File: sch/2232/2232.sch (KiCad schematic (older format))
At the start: 69 parts, among them J1 47346-0001, J2 IDC-06, J3 IDC-06, J4 IDC-10, J5 IDC-10, J6 6P6C, J7 Screw_Terminal_01x06, J8 Screw_Terminal_01x06, Q1 Q_NPN_BEC, Q2 Q_NPN_BEC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

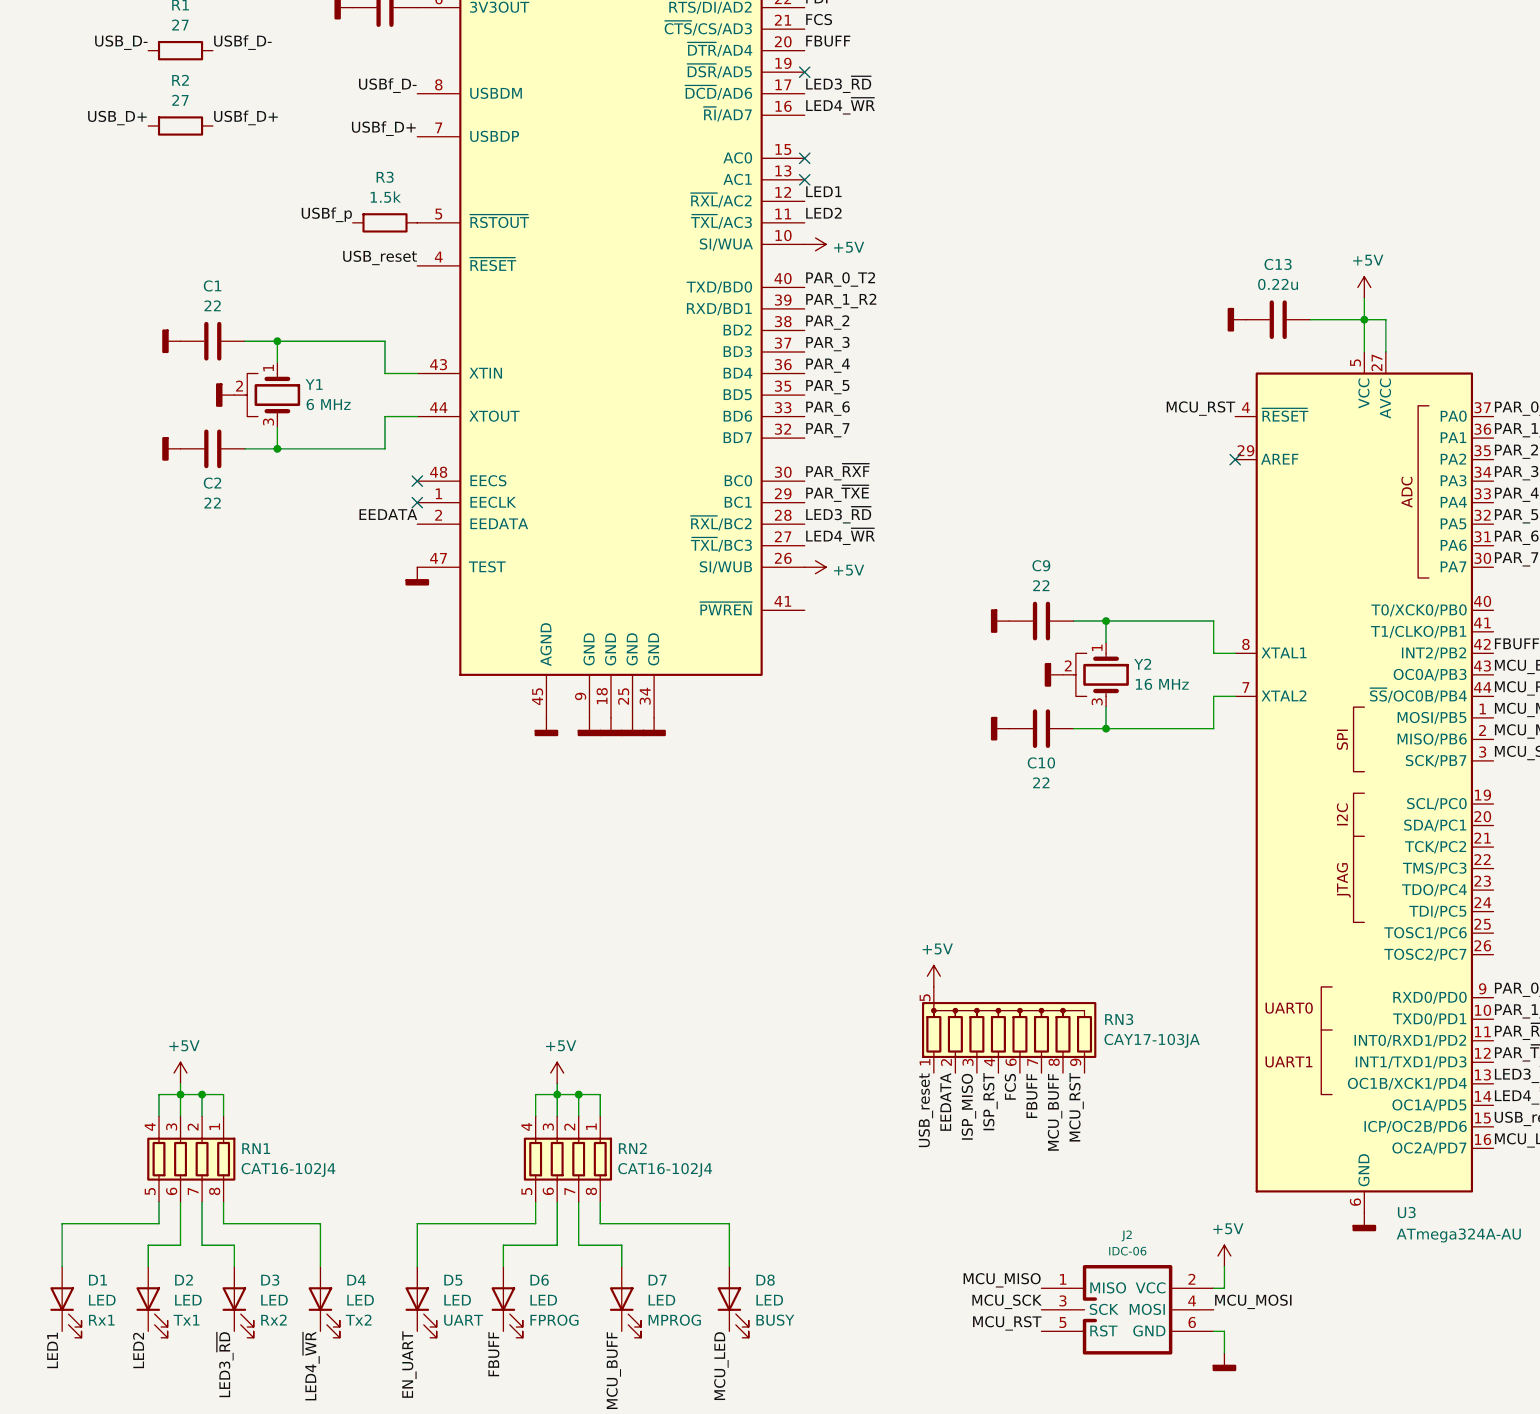
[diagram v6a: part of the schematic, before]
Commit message: UARTs routed trough connectors
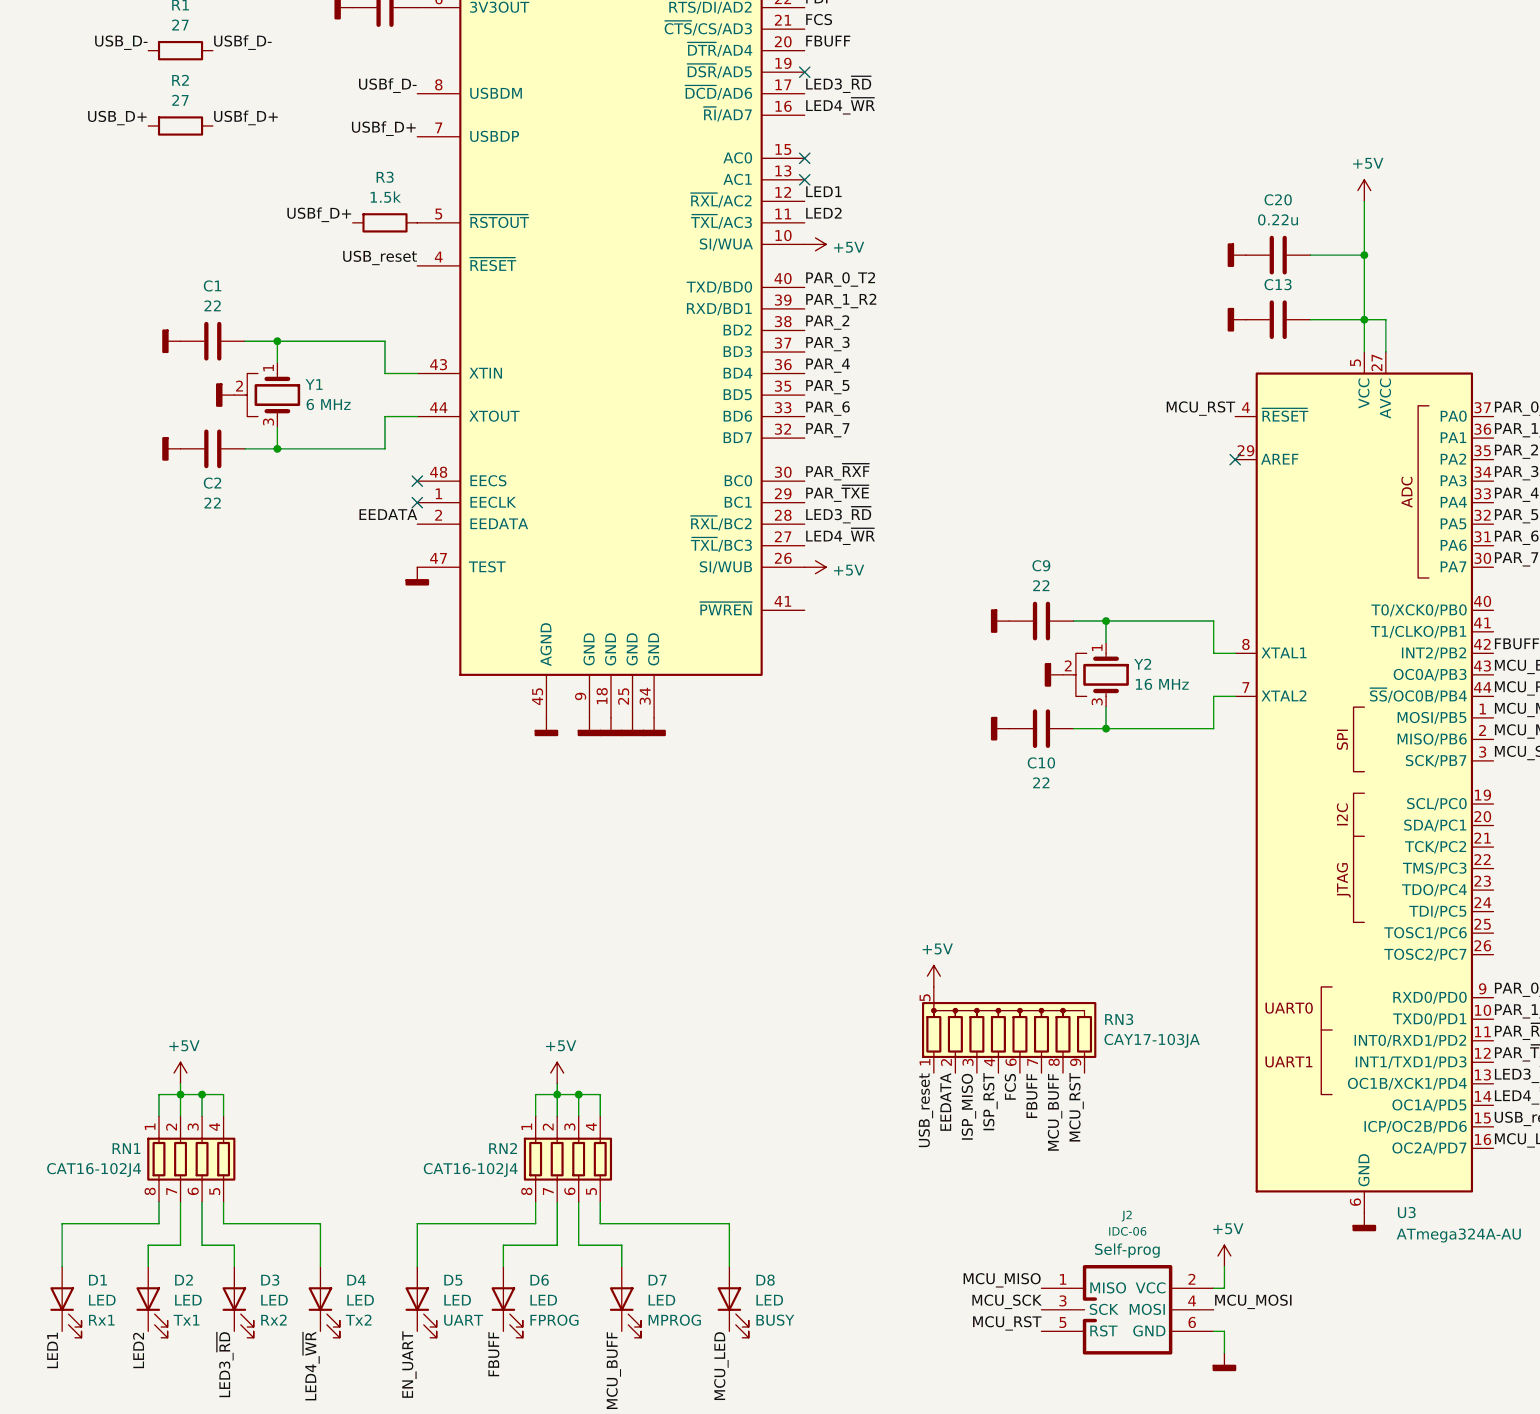
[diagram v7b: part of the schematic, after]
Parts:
- added C20: 0.22u, NevaDA:C_0603, symbol Device:C
- J2: footprint NevaDA:IDC_Header_Straight_6pins -> NevaDA:PLD-6; Role (none) -> Self-prog
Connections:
- net USBf_p is gone; now on net USBf_D+: R3.2
- net +5V: now also C20.1
- net GNDD: now also C20.2
- net at D1.2 (A): now also RN1.8 (R1.2); no longer RN1.5 (R4.2)
- net at D2.2 (A): now also RN1.7 (R2.2); no longer RN1.6 (R3.2)
- net at D3.2 (A): now also RN1.6 (R3.2); no longer RN1.7 (R2.2)
- net at D4.2 (A): now also RN1.5 (R4.2); no longer RN1.8 (R1.2)
- net at D5.2 (A): now also RN2.8 (R1.2); no longer RN2.5 (R4.2)
- net at D6.2 (A): now also RN2.7 (R2.2); no longer RN2.6 (R3.2)
- net at D7.2 (A): now also RN2.6 (R3.2); no longer RN2.7 (R2.2)
- net at D8.2 (A): now also RN2.5 (R4.2); no longer RN2.8 (R1.2)
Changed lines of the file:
@@
 	0    1    1    0
 $EndComp
-Text Label 2200 5250 2    50   ~ 0
-USBf_p
 Text Label 2500 5450 2    50   ~ 0
 USB_reset
@@
 $EndComp
 Wire Wire Line
-	6900 5600 6900 5700
+	6900 5150 6900 5400
 Wire Wire Line
 	7000 5850 7000 5700
@@
 U 1 1 5FEE100A
 P 5800 10300
-F 0 "J2" H 5800 10647 39  0000 C CNN
-F 1 "IDC-06" H 5800 10571 39  0000 C CNN
-F 2 "NevaDA:IDC_Header_Straight_6pins" H 5800 10300 39  0001 C CNN
+F 0 "J2" H 5800 10739 39  0000 C CNN
+F 1 "IDC-06" H 5800 10663 39  0000 C CNN
+F 2 "NevaDA:PLD-6" H 5800 10300 39  0001 C CNN
 F 3 "" H 5800 10300 39  0001 C CNN
+F 4 "Self-prog" H 5800 10579 50  0000 C CNN "Role"
 	1    5800 10300
 	1    0    0    -1
@@
 L power:+5V #PWR0155
 U 1 1 5FEE7711
-P 6900 5600
-F 0 "#PWR0155" H 6900 5450 50  0001 C CNN
-F 1 "+5V" H 6915 5775 50  0000 C CNN
-F 2 "" H 6900 5600 50  0001 C CNN
-F 3 "" H 6900 5600 50  0001 C CNN
-	1    6900 5600
+P 6900 5150
+F 0 "#PWR0155" H 6900 5000 50  0001 C CNN
+F 1 "+5V" H 6915 5325 50  0000 C CNN
+F 2 "" H 6900 5150 50  0001 C CNN
+F 3 "" H 6900 5150 50  0001 C CNN
+	1    6900 5150
 	1    0    0    -1
 $EndComp
@@
 U 1 1 5FEEB1B2
 P 6500 5700
-F 0 "C13" V 6245 5700 50  0000 C CNN
-F 1 "0.22u" V 6338 5700 50  0000 C CNN
+F 0 "C13" V 6339 5700 50  0000 C CNN
+F 1 "0.22u" V 6338 5700 50  0001 C CNN
 F 2 "NevaDA:C_0603" H 6538 5550 50  0001 C CNN
 F 3 "~" H 6500 5700 50  0001 C CNN
@@
 L Device:R_Pack04 RN1
 U 1 1 5FF1A659
-P 1400 9600
-F 0 "RN1" H 1120 9553 50  0000 R CNN
-F 1 "CAT16-102J4" H 1120 9646 50  0000 R CNN
-F 2 "NevaDA:R_CAT-16-4" V 1675 9600 50  0001 C CNN
-F 3 "~" H 1400 9600 50  0001 C CNN
-	1    1400 9600
-	-1   0    0    1
+P 1500 9600
+F 0 "RN1" H 1220 9553 50  0000 R CNN
+F 1 "CAT16-102J4" H 1220 9646 50  0000 R CNN
+F 2 "NevaDA:R_CAT-16-4" V 1775 9600 50  0001 C CNN
+F 3 "~" H 1500 9600 50  0001 C CNN
+	1    1500 9600
+	1    0    0    1
 $EndComp
 Text Label 850  10400 3    50   ~ 0
@@
 L Device:R_Pack04 RN2
 U 1 1 5FF34EA0
-P 3150 9600
-F 0 "RN2" H 2870 9553 50  0000 R CNN
-F 1 "CAT16-102J4" H 2870 9646 50  0000 R CNN
-F 2 "NevaDA:R_CAT-16-4" V 3425 9600 50  0001 C CNN
-F 3 "~" H 3150 9600 50  0001 C CNN
-	1    3150 9600
-	-1   0    0    1
+P 3250 9600
+F 0 "RN2" H 2970 9553 50  0000 R CNN
+F 1 "CAT16-102J4" H 2970 9646 50  0000 R CNN
+F 2 "NevaDA:R_CAT-16-4" V 3525 9600 50  0001 C CNN
+F 3 "~" H 3250 9600 50  0001 C CNN
+	1    3250 9600
+	1    0    0    1
 $EndComp
 Text Label 3450 10400 3    50   ~ 0
@@
 	1    0    0    -1
 $EndComp
+$Comp
+L Device:C C20
+U 1 1 5FDC0413
+P 6500 5400
+F 0 "C20" V 6245 5400 50  0000 C CNN
+F 1 "0.22u" V 6338 5400 50  0000 C CNN
+F 2 "NevaDA:C_0603" H 6538 5250 50  0001 C CNN
+F 3 "~" H 6500 5400 50  0001 C CNN
+	1    6500 5400
+	0    1    1    0
+$EndComp
+$Comp
+L power:GNDD #PWR0163
+U 1 1 5FDC042B
+P 6350 5400
+F 0 "#PWR0163" H 6350 5150 50  0001 C CNN
+F 1 "GNDD" V 6354 5290 50  0001 R CNN
+F 2 "" H 6350 5400 50  0001 C CNN
+F 3 "" H 6350 5400 50  0001 C CNN
+	1    6350 5400
+	0    1    1    0
+$EndComp
+Wire Wire Line
+	6650 5400 6900 5400
+Connection ~ 6900 5400
+Wire Wire Line
+	6900 5400 6900 5700
+Text Label 2200 5250 2    50   ~ 0
+USBf_D+
 $EndSCHEMATC

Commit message: All components on-board
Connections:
- net EN_UART: now also U3.21 (TCK/PC2)
- net IDC_CLK: now also RN5.7 (R2.2); no longer RN5.6 (R3.2)
- net IDC_MISO: now also RN5.6 (R3.2); no longer RN5.5 (R4.2)
- net IDC_MOSI: now also RN5.5 (R4.2); no longer RN5.8 (R1.2)
- net IDC_RST: now also RN5.8 (R1.2); no longer RN5.7 (R2.2)
- net ISP_CLK: now also RN5.2 (R2.1); no longer RN5.3 (R3.1)
- net ISP_MISO: now also RN5.3 (R3.1); no longer RN5.4 (R4.1)
- net ISP_MOSI: now also RN5.4 (R4.1); no longer RN5.1 (R1.1)
- net ISP_RST: now also RN5.1 (R1.1); no longer RN5.2 (R2.1)
- net MCU_BUFF: now also U3.22 (TMS/PC3); no longer U3.43 (OC0A/PB3)
- net RX1_3V: now also RN6.3 (R3.1); no longer RN6.2 (R2.1)
- net RX1_3VR: now also RN6.6 (R3.2); no longer RN6.7 (R2.2)
- net RX2_3V: now also RN6.1 (R1.1); no longer RN6.4 (R4.1)
- net RX2_3VR: now also RN6.8 (R1.2); no longer RN6.5 (R4.2)
- net TX1_3V: now also RN6.4 (R4.1); no longer RN6.1 (R1.1)
- net TX1_3VR: now also RN6.5 (R4.2); no longer RN6.8 (R1.2)
- net TX2_3V: now also RN6.2 (R2.1); no longer RN6.3 (R3.1)
- net TX2_3VR: now also RN6.7 (R2.2); no longer RN6.6 (R3.2)
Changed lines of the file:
@@
 L Device:R_Pack04 RN6
 U 1 1 5FDFDC7F
-P 13900 5250
-F 0 "RN6" V 13480 5250 50  0000 C CNN
-F 1 "CAT16-471J4" V 13573 5250 50  0000 C CNN
-F 2 "NevaDA:R_CAT-16-4" V 14175 5250 50  0001 C CNN
-F 3 "~" H 13900 5250 50  0001 C CNN
-	1    13900 5250
-	0    1    1    0
+P 13900 5150
+F 0 "RN6" V 14229 5150 50  0000 C CNN
+F 1 "CAT16-471J4" V 14136 5150 50  0000 C CNN
+F 2 "NevaDA:R_CAT-16-4" V 14175 5150 50  0001 C CNN
+F 3 "~" H 13900 5150 50  0001 C CNN
+	1    13900 5150
+	0    1    -1   0
 $EndComp
 Text Label 14550 5150 2    50   ~ 0
@@
 	0    1    1    0
 $EndComp
+Text Label 11250 3800 0    50   ~ 0
+IDC_MISO
+Text Label 11250 3700 0    50   ~ 0
+IDC_CLK
+Text Label 11250 3600 0    50   ~ 0
+IDC_RST
 Text Label 11250 3900 0    50   ~ 0
-IDC_MISO
-Text Label 11250 3800 0    50   ~ 0
-IDC_CLK
-Text Label 11250 3700 0    50   ~ 0
-IDC_RST
-Text Label 11250 3600 0    50   ~ 0
 IDC_MOSI
+Text Label 10850 3800 2    50   ~ 0
+ISP_MISO
+Text Label 10850 3700 2    50   ~ 0
+ISP_CLK
+Text Label 10850 3600 2    50   ~ 0
+ISP_RST
 Text Label 10850 3900 2    50   ~ 0
-ISP_MISO
-Text Label 10850 3800 2    50   ~ 0
-ISP_CLK
-Text Label 10850 3700 2    50   ~ 0
-ISP_RST
-Text Label 10850 3600 2    50   ~ 0
 ISP_MOSI
 Text Label 8250 4000 2    50   ~ 0
@@
 Text Label 8250 4500 2    50   ~ 0
 MCU_ROUT
-Text Label 7500 7350 0    50   ~ 0
+Text Label 7500 8250 0    50   ~ 0
 MCU_BUFF
 Text Label 8250 4800 2    50   ~ 0
@@
 Text Label 2200 5250 2    50   ~ 0
 USBf_D+
+Text Label 7500 8150 0    50   ~ 0
+EN_UART
 $EndSCHEMATC
